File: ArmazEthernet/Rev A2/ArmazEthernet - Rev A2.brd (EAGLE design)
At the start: 72 x 80 mm, 123 parts, among them J1 22-05-7028-02, P1 RB1-125BAG1A, U1 LM317MDCY, U2 LM317MDCY, U3 KSZ8995MA, U4 AT24C02C-SSHM-B, X1 NE8FAV, X2 NE8FAV, Y1 8Z-25.000MHZMAAJ-T

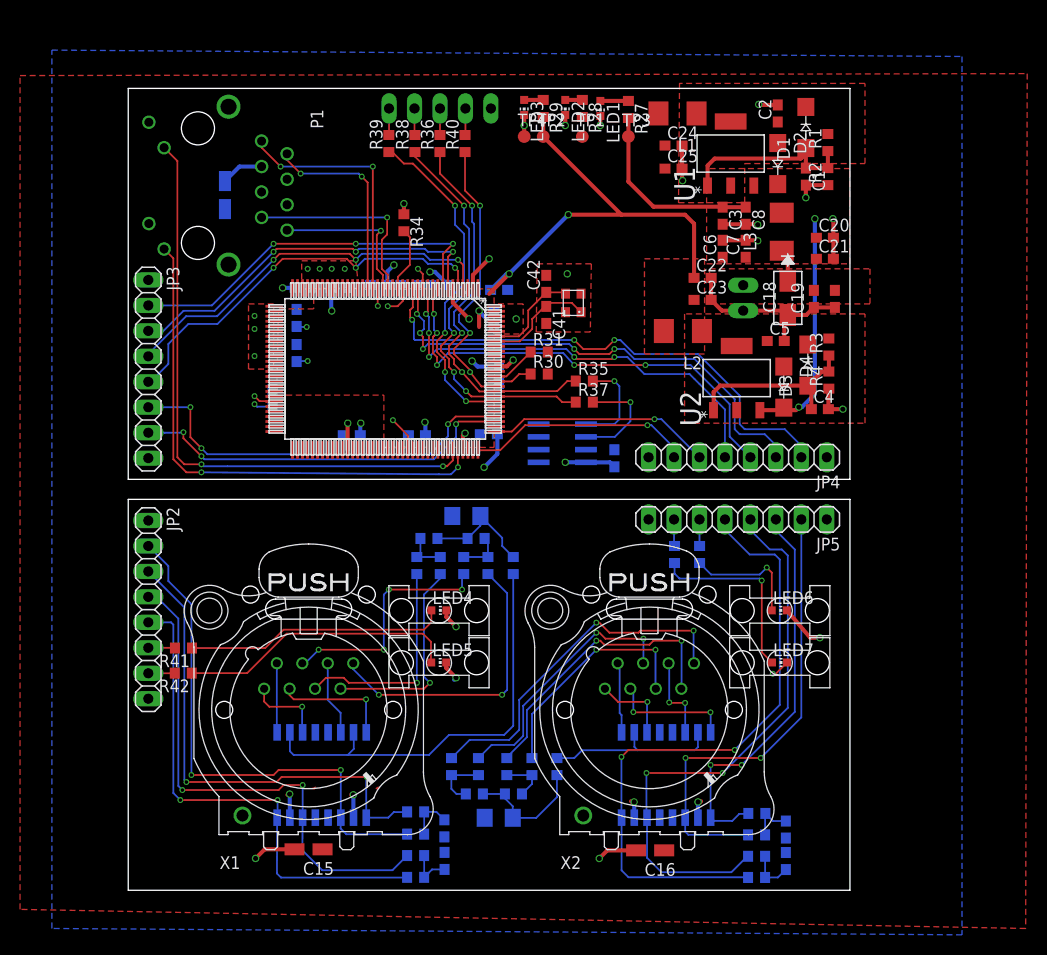
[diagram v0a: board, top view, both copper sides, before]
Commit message: Fix angle wire on the board
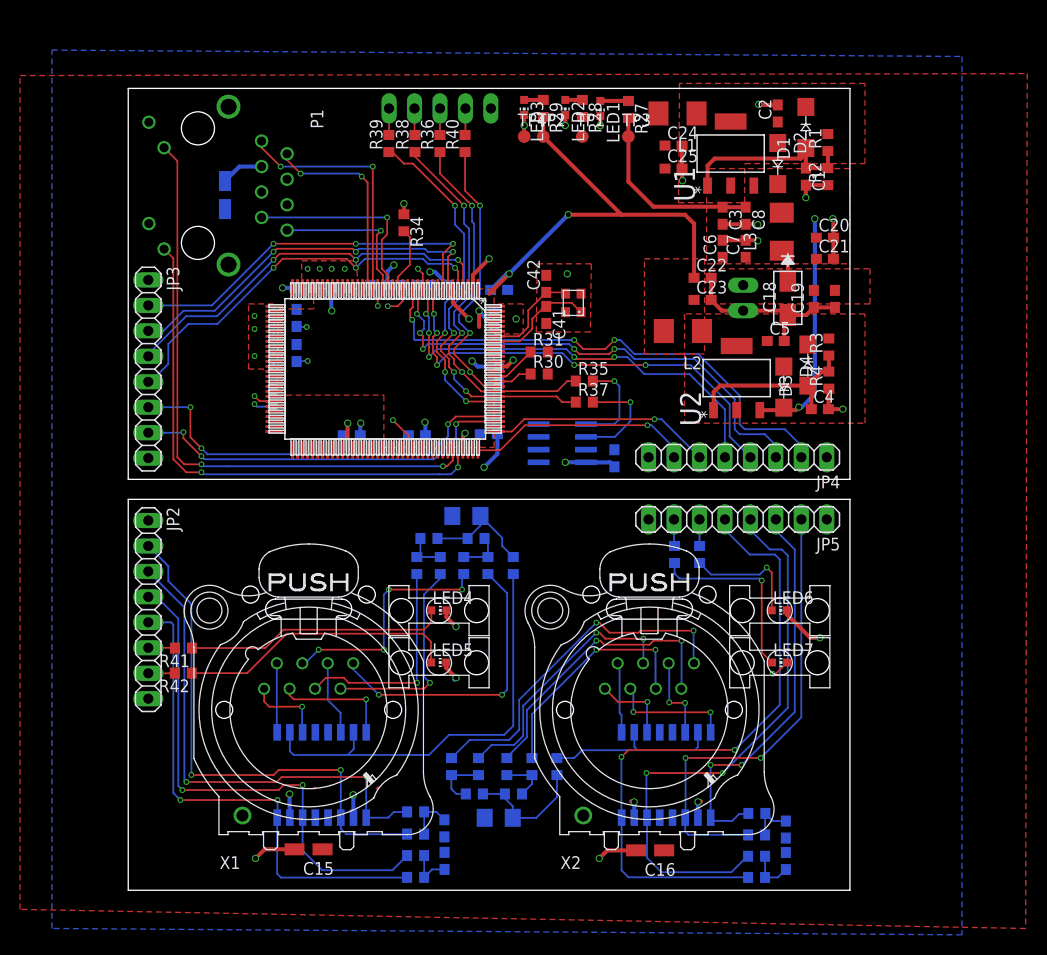
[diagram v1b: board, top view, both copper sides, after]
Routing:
- net RX1P_ISO: track 91.6 -> 90.8 mm

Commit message: Update board
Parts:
- added C33, C44: 0.1uF, rcl:C0603
- added R32, R33, R45, R46: 49.9, rcl:R0603
- added U$5, U$8: EXMACHINA-LOGO-NAME, exmachina:EXM-LOGO-BASELINE
- added U$6, U$7: CC-BY-SA, cc-by-sa:CC-BY-SA
- moved LED7 0.23 mm to (65.0, 22.5)
- moved LED5 0.23 mm to (31.0, 22.5)
- moved U$2 0.20 mm to (65.0, 22.5)
- moved U$4 0.20 mm to (31.0, 22.5)
- moved U$1 0.10 mm to (65.0, 28.0)
- moved U$3 0.10 mm to (31.0, 28.0)
- moved LED6 0.09 mm to (65.0, 28.0)
- moved LED4 0.08 mm to (31.0, 28.0)
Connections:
- net RX1+ renamed RX1_P
- net RX1- renamed RX1_M
- net RX1M_ISO renamed RX1_ISO_M
- net RX1P_ISO renamed RX1_ISO_P
- net RX2+ renamed RX2_P
- net RX2- renamed RX2_M
- net RX2M_ISO renamed RX2_ISO_M
- net RX2P_ISO renamed RX2_ISO_P
- net TX1+ renamed TX1_P
- net TX1- renamed TX1_M
- net TX1M_ISO renamed TX1_ISO_M
- net TX1P_ISO renamed TX1_ISO_P
- net TX2+ renamed TX2_P
- net TX2- renamed TX2_M
- net TX2M_ISO renamed TX2_ISO_M
- net TX2P_ISO renamed TX2_ISO_P
- removed net RX3M_ISO: P1.R8, U3.20
- removed net RX3P_ISO: P1.R7, U3.19
- removed net TX3M_ISO: P1.R2, U3.23
- removed net TX3P_ISO: P1.R1, U3.22
- new net N$27: C33.1, R32.1, R33.1
- new net N$31: C44.1, R45.1, R46.1
- new net RX3_ISO_M: P1.R8, R46.2, U3.20
- new net RX3_ISO_P: P1.R7, R45.2, U3.19
- new net TX3_ISO_M: P1.R2, R33.2, U3.23
- new net TX3_ISO_P: P1.R1, R32.2, U3.22
- net GND: now also C33.2, C44.2
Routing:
- net TX3_ISO_P: track 0.00 -> 28.9 mm, vias 0 -> 2
- net TX3P_ISO: track 24.6 -> 0.00 mm, vias 2 -> 0
- net TX3_ISO_M: track 0.00 -> 22.9 mm, vias 0 -> 2
- net RX3_ISO_P: track 0.00 -> 21.4 mm, vias 0 -> 2
- net TX3M_ISO: track 20.1 -> 0.00 mm, vias 2 -> 0
- net RX3P_ISO: track 20.0 -> 0.00 mm, vias 1 -> 0
- net RX3_ISO_M: track 0.00 -> 16.8 mm, vias 0 -> 2
- net RX3M_ISO: track 15.5 -> 0.00 mm, vias 1 -> 0
- net +1V8: track 57.6 -> 62.2 mm, vias 8 -> 9
- net N$31: track 0.00 -> 4.20 mm
- net N$27: track 0.00 -> 4.20 mm
- net GND: track 94.1 -> 97.5 mm, vias 36 -> 38
- net N$1: vias 0 -> 2
- net N$8: vias 2 -> 4

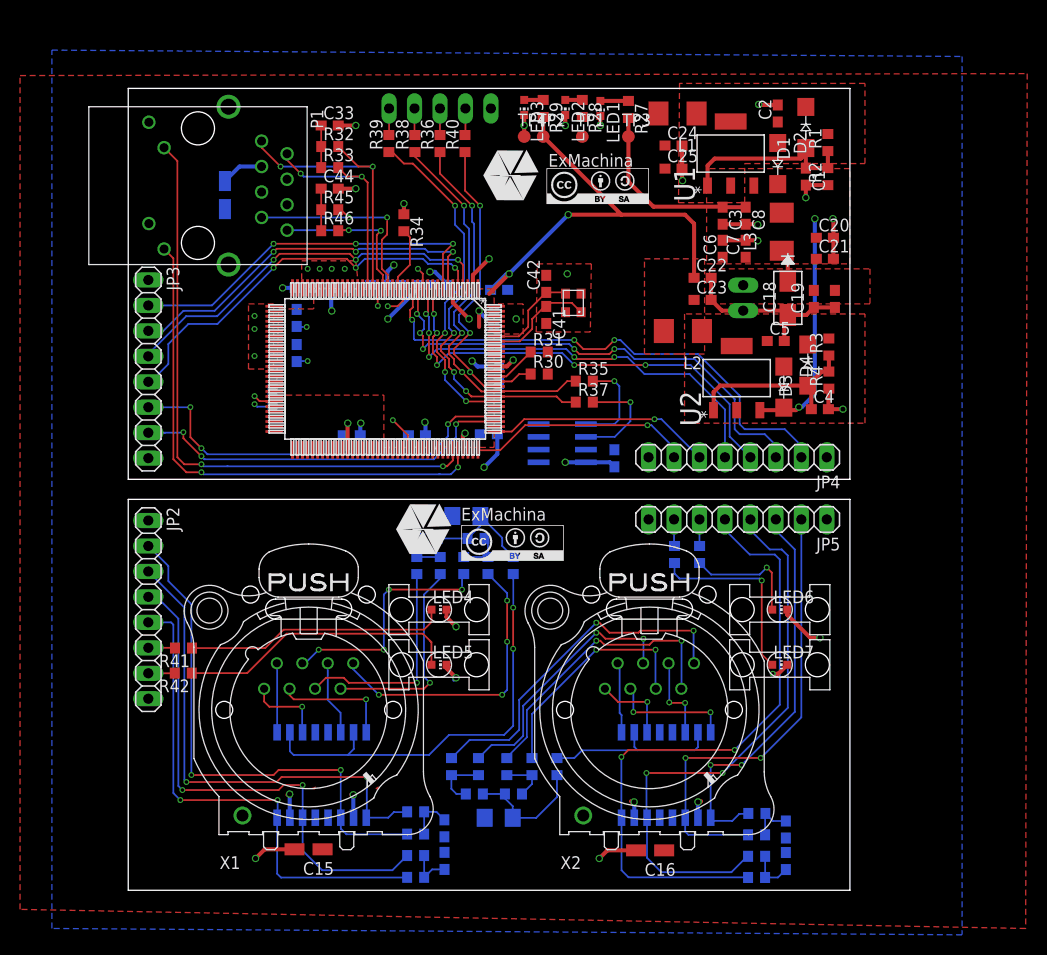
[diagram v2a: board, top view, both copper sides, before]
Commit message: Modify board disposition
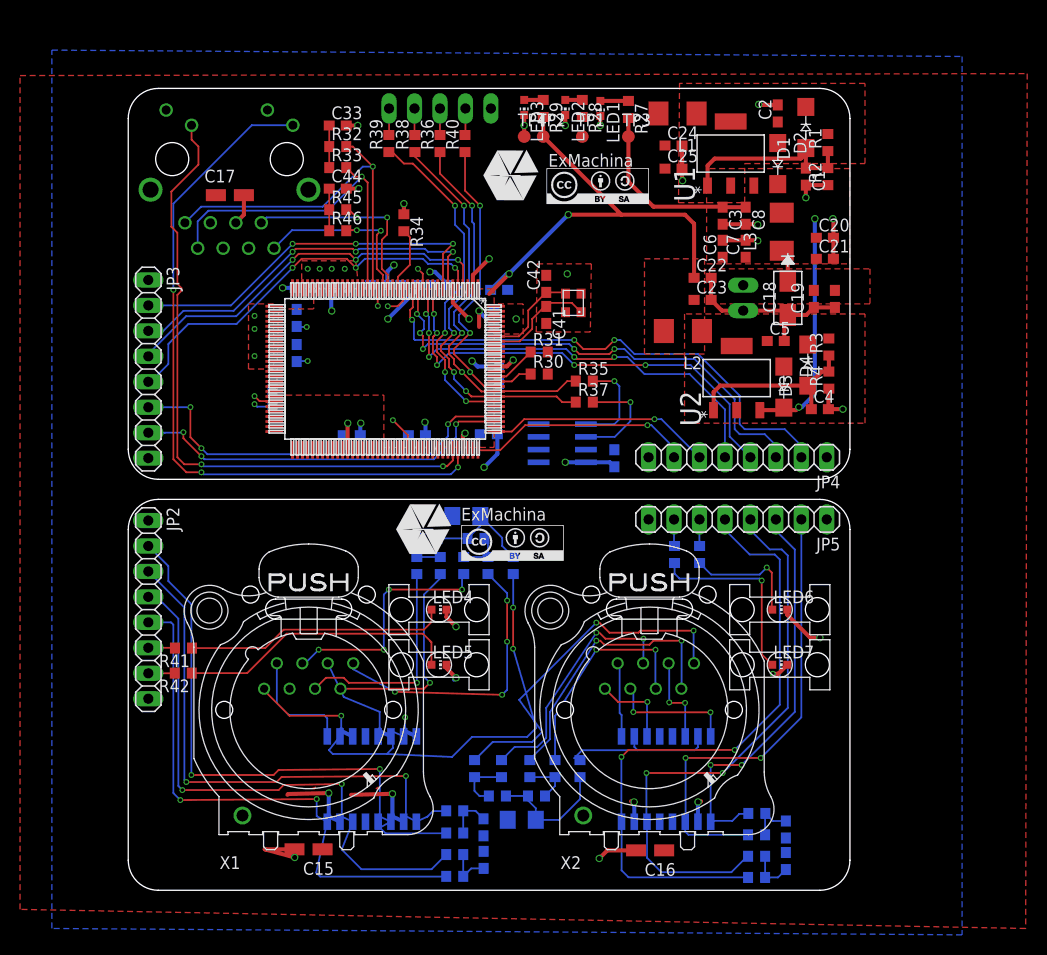
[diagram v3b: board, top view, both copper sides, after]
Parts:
- moved T1 5.02 mm to (24.3, 11.1)
- moved P1 4.11 mm to (10.1, 72.9), flipped to the bottom, turned to 180 degrees
- moved C9 3.90 mm to (35.4, 6.28)
- moved C10 3.90 mm to (35.5, 3.03)
- moved R19 3.90 mm to (32.6, 5.70)
- moved R20 3.90 mm to (32.6, 7.92)
- moved R21 3.90 mm to (32.6, 1.39)
- moved R22 3.90 mm to (32.6, 3.56)
- moved R16 2.31 mm to (37.2, 12.1)
- moved C11 2.31 mm to (39.3, 7.03)
- moved R12 2.31 mm to (40.1, 12.1)
- moved R13 2.31 mm to (45.1, 12.1)
- moved R14 2.31 mm to (42.6, 12.1)
- moved R15 2.31 mm to (40.7, 9.41)
- moved R7 2.31 mm to (36.8, 9.41)
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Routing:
- net L3-1: track 52.4 -> 71.8 mm, vias 2 -> 3
- net TX3_ISO_M: track 22.9 -> 34.2 mm, vias 2 -> 1
- net TX1_P: track 11.7 -> 2.61 mm
- net TX3_ISO_P: track 28.9 -> 36.7 mm, vias 2 -> 1
- net +3V3: track 31.7 -> 38.5 mm
- net TX1_ISO_M: track 90.2 -> 95.5 mm
- net RX1_ISO_P: track 90.8 -> 95.6 mm
- net RX1_ISO_M: track 90.7 -> 95.4 mm
- net RX1_M: track 7.14 -> 11.4 mm
- net TX1_ISO_P: track 87.3 -> 91.3 mm
- net RX1_P: track 7.86 -> 11.7 mm
- net GND: track 97.5 -> 101.3 mm
- net L3-2: track 60.6 -> 64.3 mm
- net TX1_M: track 7.43 -> 10.8 mm
- net RX3_ISO_M: track 16.8 -> 18.8 mm
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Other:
- outline, holes or cut-outs redrawn

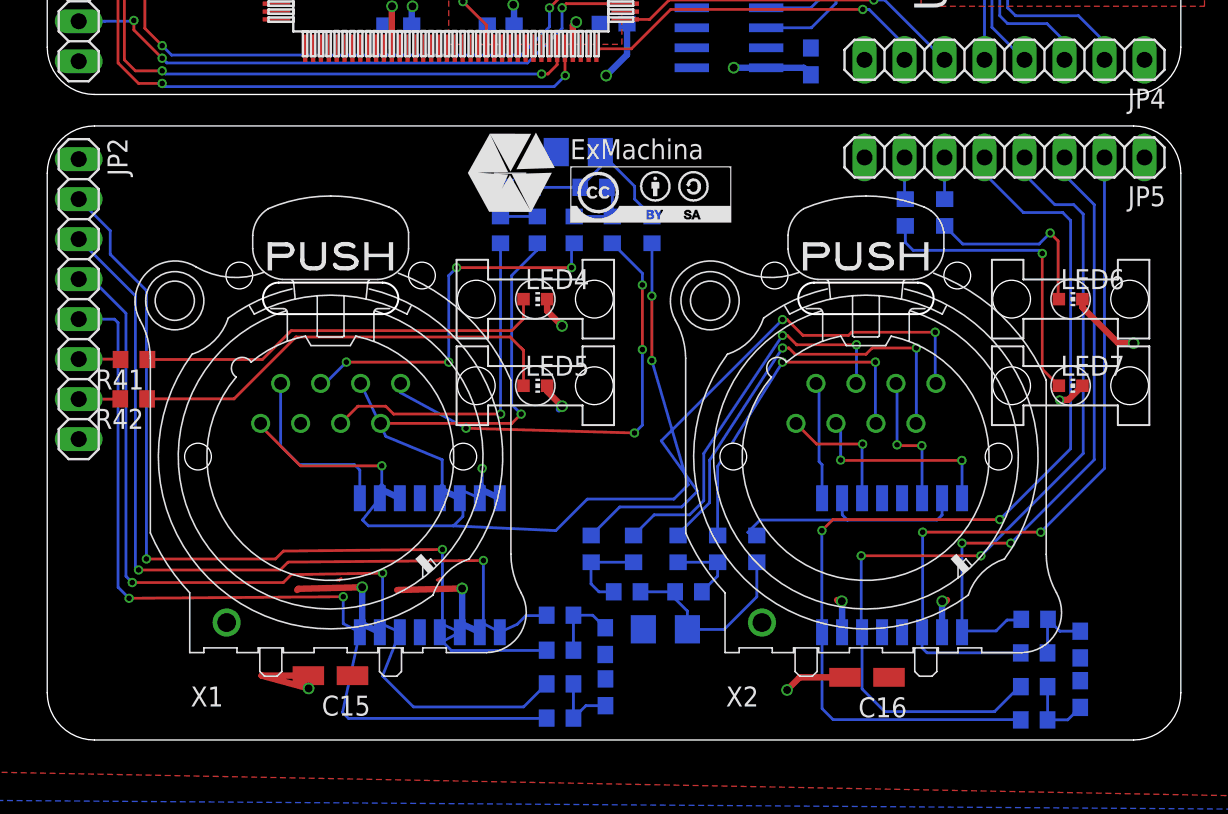
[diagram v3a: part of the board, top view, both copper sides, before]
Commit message: Panel the board
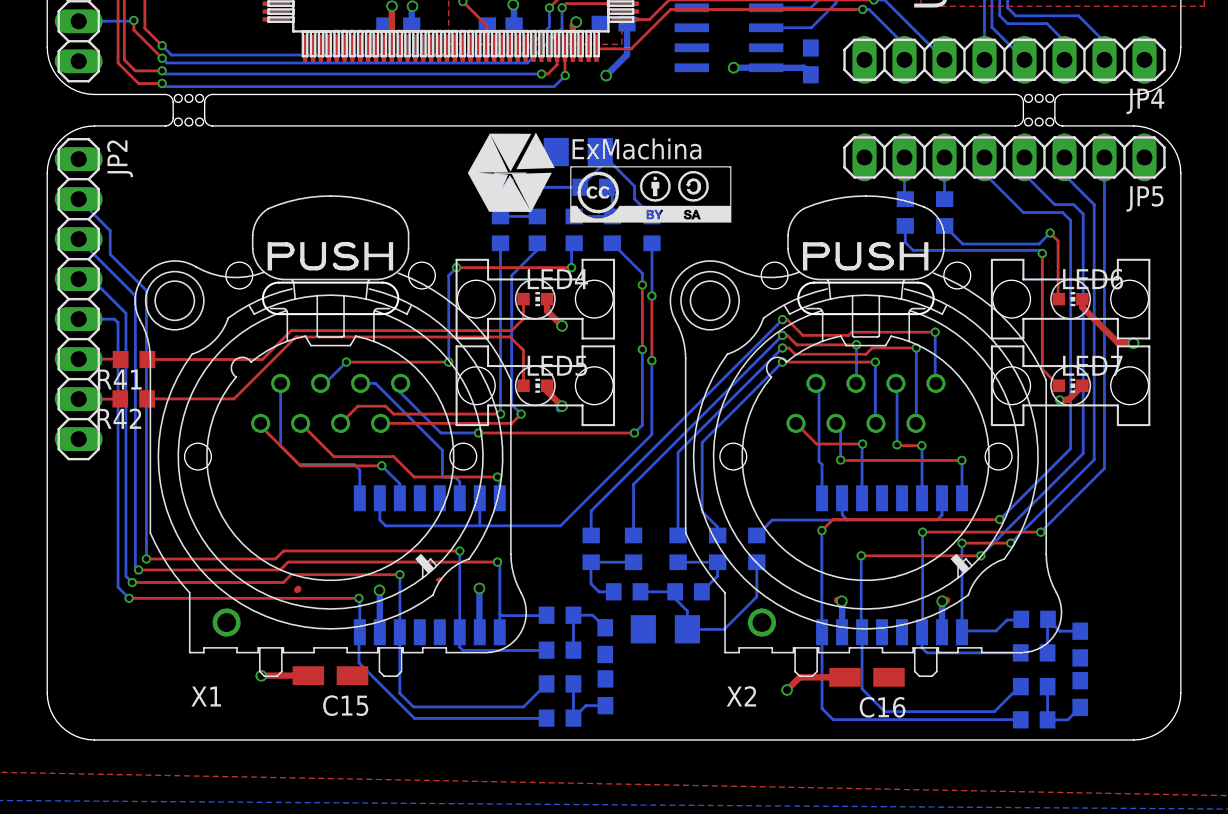
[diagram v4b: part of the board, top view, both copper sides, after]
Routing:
- net TX1_P: track 2.61 -> 15.3 mm
- net +3V3: track 38.5 -> 28.4 mm
- net N$1: track 43.2 -> 35.1 mm
- net N$5: track 36.2 -> 32.2 mm
- net GND: track 101.3 -> 98.2 mm
- net RX1_ISO_M: track 95.4 -> 92.7 mm
- net N$4: track 16.8 -> 15.3 mm
- net N$18: track 22.0 -> 23.3 mm
- net TX1_ISO_M: track 95.5 -> 94.3 mm
- net N$15: track 24.8 -> 24.0 mm
- net N$12: track 27.7 -> 28.4 mm
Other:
- outline, holes or cut-outs redrawn

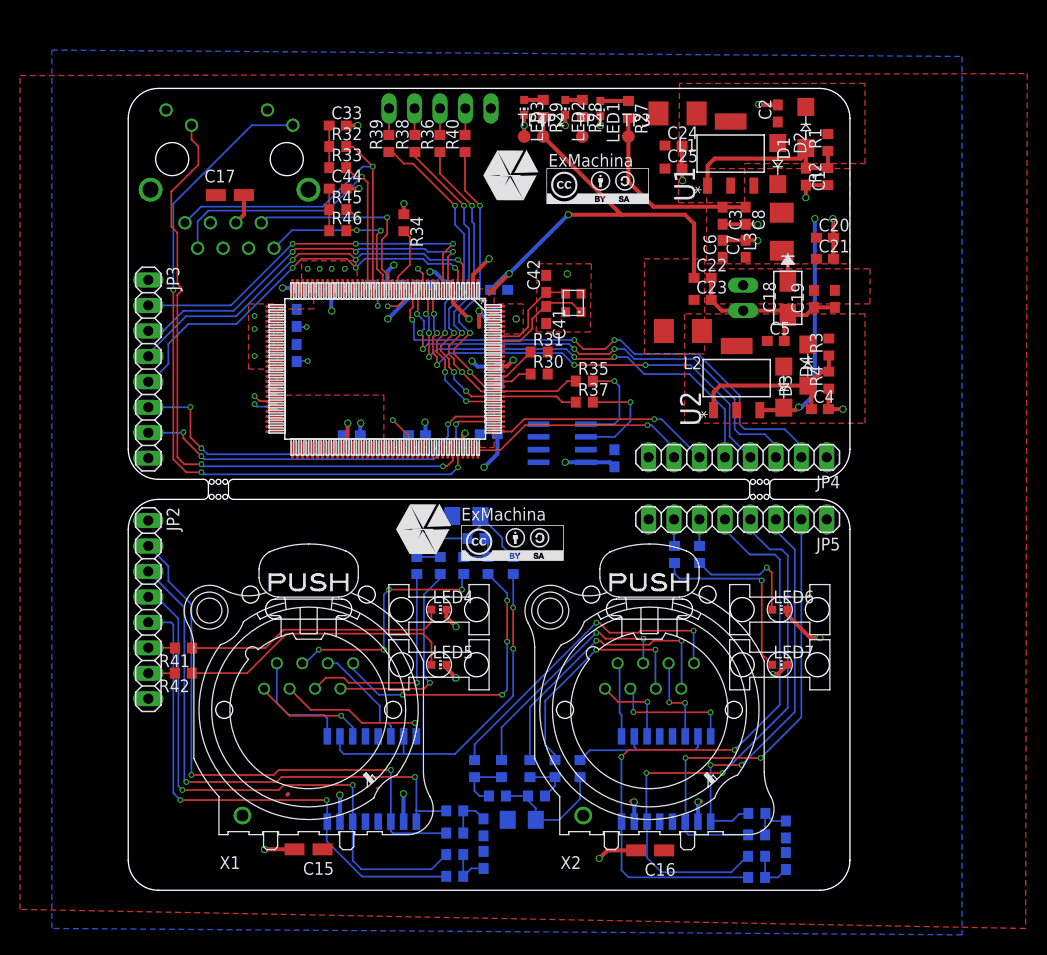
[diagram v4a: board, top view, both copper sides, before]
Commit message: Turn JP2 Add res to L3 Add reset circuit Add rev to the silkscreen Add Keepout near the transfo
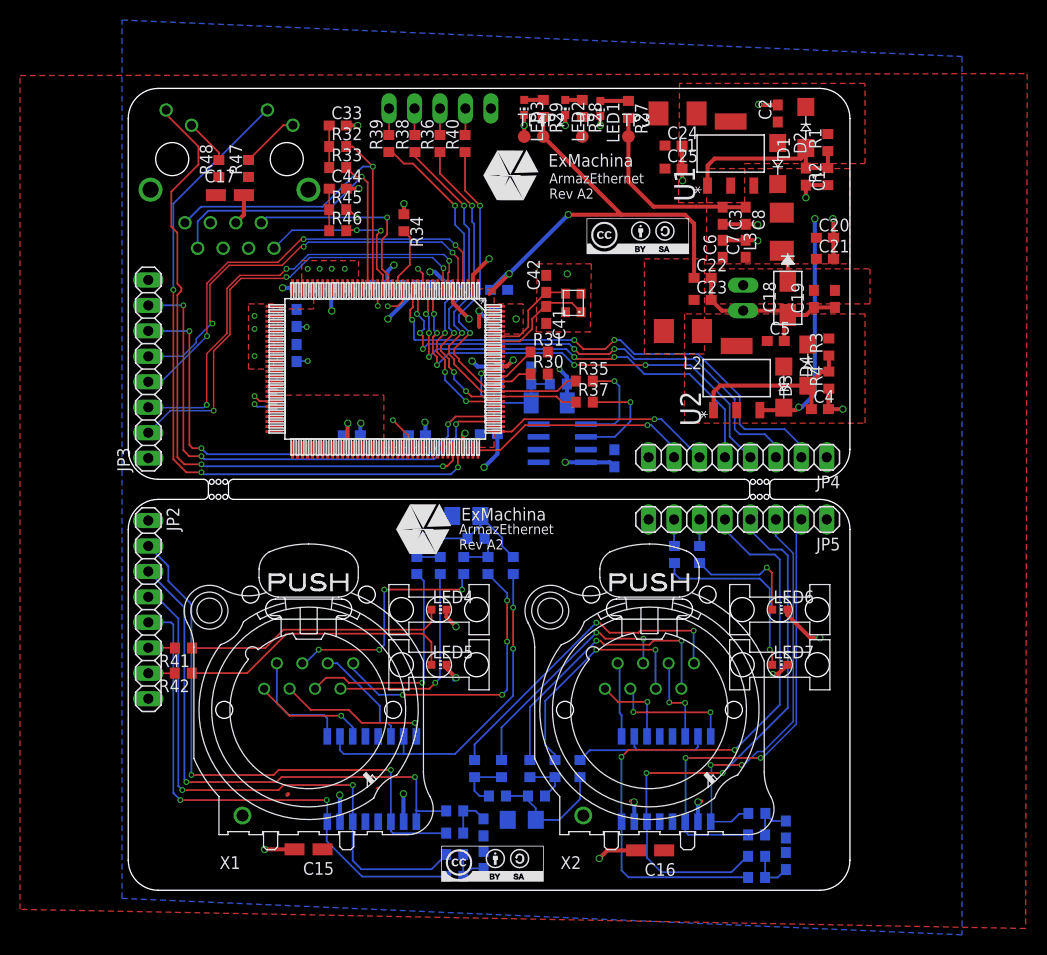
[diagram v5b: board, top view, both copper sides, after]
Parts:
- removed U$7: CC-BY-SA, cc-by-sa:CC-BY-SA
- added C45: 10uF, rcl:C0603
- added R47, R48: 220, rcl:R0603
- added R49: 10K, rcl:R0603
- added U$10: CC-BY-SA, cc-by-sa:CC-BY-SA
- added U$9: 1N4148W, diode:SOD-123_MINI-SMA
- moved U$6 6.40 mm to (51.0, 65.7)
- turned JP3 to 90 degrees
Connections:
- net RX1_ISO_M renamed RX1_ISO_N
- net RX2_ISO_M renamed RX2_ISO_N
- net RX3_ISO_M renamed RX3_ISO_N
- net TX1_ISO_M renamed TX1_ISO_N
- net TX2_ISO_M renamed TX2_ISO_N
- net TX3_ISO_M renamed TX3_ISO_N
- new net N$34: P1.L3, R48.2
- new net N$35: P1.L1, R47.2
- net +3V3: now also R47.1, R48.1, R49.2, U$9.C
- net GND: now also C45.2; no longer P1.L2, P1.L4
- net L3-1: now also P1.L2; no longer P1.L1
- net L3-2: now also P1.L4; no longer P1.L3
- net RST_N: now also C45.1, R49.1, U$9.A
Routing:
- net L1-2: track 41.2 -> 54.5 mm
- net RST_N: track 0.00 -> 12.8 mm, vias 0 -> 1
- net L1-1: track 43.4 -> 51.4 mm
- net TX1_ISO_N: track 94.3 -> 101.7 mm
- net TX1_ISO_P: track 91.1 -> 98.2 mm
- net N$35: track 0.00 -> 5.86 mm
- net RX1_ISO_P: track 95.2 -> 100.7 mm
- net N$34: track 0.00 -> 4.60 mm
- net +3V3: track 28.4 -> 32.1 mm, vias 11 -> 12
- net L3-2: track 64.3 -> 66.8 mm
- net RX1_ISO_N: track 92.7 -> 94.7 mm
- net L3-1: track 71.8 -> 69.8 mm
- net N$11: track 21.7 -> 22.6 mm
- net SPIS-N: vias 3 -> 2
- net SDA: vias 3 -> 2
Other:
- board text added: "ArmazEthernet Rev A2"
